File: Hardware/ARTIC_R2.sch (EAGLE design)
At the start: 114 parts, among them J1 U.FL, J2 THING_PLUS, J5 Flash Programming, K1 TLP3475R, Q1 3.1A/30V/105mΩ, U1 2Mbit SPI Flash, U2 1.8V/100mA, U3 ARTIC_R2, U4 RFPA0133, U5 AS179-92LF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

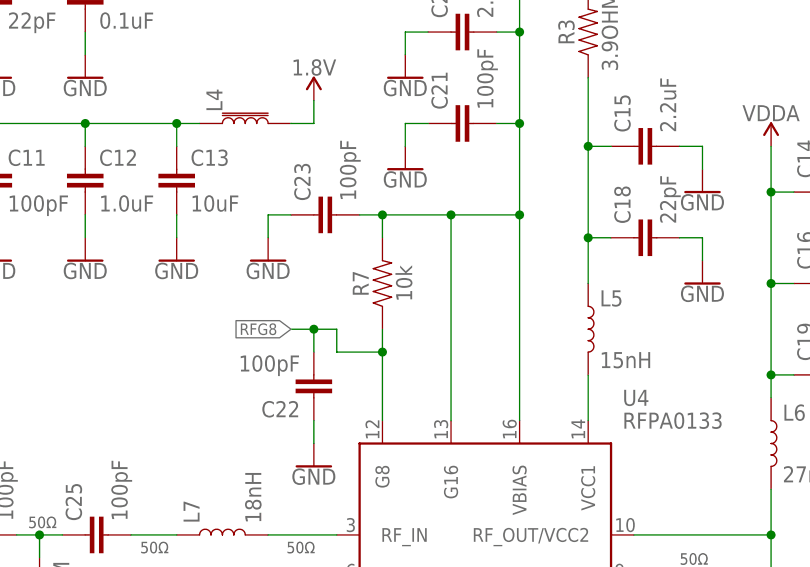
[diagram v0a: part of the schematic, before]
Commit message: Changing R7 from 10K to 1K
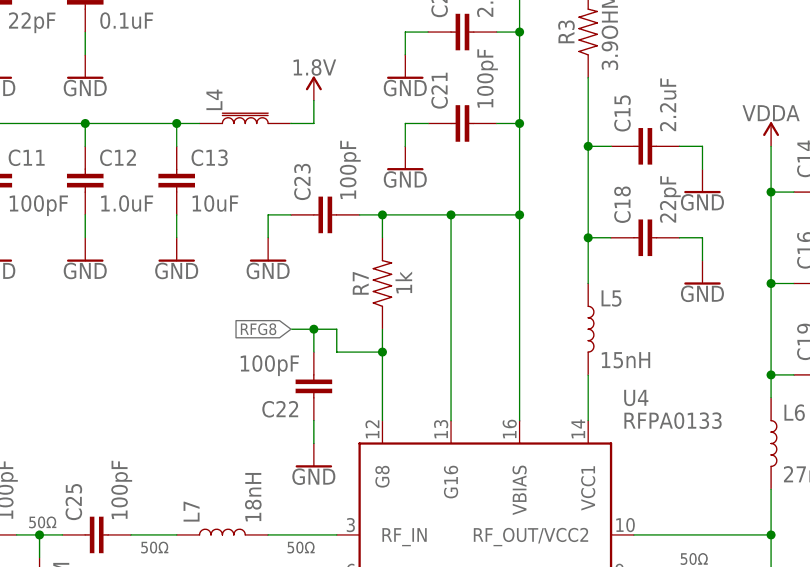
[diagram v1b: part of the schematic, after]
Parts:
- R7: value 10k -> 1k; device SparkFun-Resistors:10KOHM-0402T-1/16W-1% -> SparkFun-Resistors:1KOHM-0402T-1/16W-1%
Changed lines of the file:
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@@
 <part name="L7" library="New_Parts_Coils" deviceset="18NH" device="-0402" value="18nH"/>
 <part name="GND33" library="SparkFun-PowerSymbols" deviceset="GND" device=""/>
-<part name="R7" library="SparkFun-Resistors" deviceset="10KOHM" device="-0402T-1/16W-1%" value="10k"/>
+<part name="R7" library="SparkFun-Resistors" deviceset="1KOHM" device="-0402T-1/16W-1%" value="1k"/>
 <part name="C23" library="SparkFun-Capacitors" deviceset="100PF" device="-0402T-50V-5%" value="100pF"/>
 <part name="C22" library="SparkFun-Capacitors" deviceset="100PF" device="-0402T-50V-5%" value="100pF"/>

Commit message: Updates for X03. Design now includes a 3.0V regulator for the RF amp gain and bias.
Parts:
- removed JP7: JUMPER-SMT_2_NO_SILK, SparkFun-Jumpers:JUMPER-SMT_2_NO_SILK
- added R14: 470, New_Parts_Resistors:470OHM-0402-TIGHT-1/16W-1%
- added R17: 47, New_Parts_Resistors:47OHM-0402-TIGHT-1/16W-1%
- added TP4: TEST-POINTTP_15TH_THRU, SparkFun-Connectors:TEST-POINTTP_15TH_THRU
- added U6: 3.0V, New_Parts_IC-Power:V_REG_LP5907SOT23-3.0V
- R1, R16: value 100k -> 10k; device SparkFun-Resistors:100KOHM-0402T-1/16W-1% -> SparkFun-Resistors:10KOHM-0402T-1/16W-1%
- R7: value 1k -> 10k; device SparkFun-Resistors:1KOHM-0402T-1/16W-1% -> SparkFun-Resistors:10KOHM-0402T-1/16W-1%
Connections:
- new net PD: C43.2, C44.1, R14.2, R17.2, U4.PD
- new net VREF1: C20.2, C21.2, C23.1, K1.DRAIN_1, TP4.1, U4.G16, U4.VBIAS, U6.OUT
- net G8: no longer JP7.1
- net GND: now also C23.2, R14.1, R7.2, U6.GND; no longer C23.1, K1.DRAIN_1
- net PA_PD: now also R17.1; no longer C43.2, C44.1, U4.PD
- net RFG8: no longer JP7.2
- net VDDA: now also U6.EN, U6.IN; no longer C20.2, C21.2, C23.2, R7.2, U4.G16, U4.VBIAS
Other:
- note added: "Decoupled by C47 and C20"
- note added: "LP5907-3.0V ------------- Iout (max): 250mA Vin (max): 5.5V Vdrop (max): 250mV Iq (max): 1uA"
- note added: "Power Switching & Voltage Regulation"
- note added: "SP6214-1.8V ------------- Iout (max): 100mA Vin (max): 7.0V Vdrop (max): 250mV Iq: 65uA"
- note added: "X03"
- note removed: "1.8V Regulator"
- note removed: "Power Switching & 3.3V Regulation"
- note removed: "SP6214-1.8V ---------------- Iout (max): 100mA Vin (max): 7.0V Vdrop (max): 250mV Iq: 65uA"
- note removed: "X02"
- moved on the sheet: C1, C20, C21, C22, C23, C24, C25, C3, C4, C43, C44, C47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

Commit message: Final tweaks for X03. Changed 8dB to G8. Increased annular ring to 3.5mil.
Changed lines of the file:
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@@
 <wire x1="378.46" y1="205.74" x2="378.46" y2="279.4" width="0.2032" layer="97" style="longdash"/>
 <wire x1="99.06" y1="68.58" x2="0" y2="68.58" width="0.2032" layer="97" style="longdash"/>
-<text x="6.604" y="259.842" size="5.08" layer="97">Power Switching &amp; Voltage
+<text x="6.604" y="259.842" size="5.08" layer="94">Power Switching &amp; Voltage
 Regulation</text>
-<text x="157.48" y="213.36" size="5.08" layer="97">Flash Memory</text>
-<text x="299.72" y="213.36" size="5.08" layer="97">Antenna Switch</text>
-<text x="391.16" y="213.36" size="5.08" layer="97">Antenna</text>
-<text x="167.64" y="30.48" size="5.08" layer="97">ARTIC R2</text>
-<text x="327.66" y="81.28" size="5.08" layer="97">RF Amp</text>
-<text x="43.18" y="5.08" size="5.08" layer="97">Pins</text>
+<text x="157.48" y="213.36" size="5.08" layer="94">Flash Memory</text>
+<text x="299.72" y="213.36" size="5.08" layer="94">Antenna Switch</text>
+<text x="391.16" y="213.36" size="5.08" layer="94">Antenna</text>
+<text x="167.64" y="30.48" size="5.08" layer="94">ARTIC R2</text>
+<text x="327.66" y="81.28" size="5.08" layer="94">RF Amp</text>
+<text x="43.18" y="5.08" size="5.08" layer="94">Pins</text>
 <text x="258.572" y="82.042" size="1.27" layer="97">50Ω</text>
 <text x="285.75" y="76.962" size="1.27" layer="97">50Ω</text>
@@
 <text x="401.574" y="249.428" size="1.27" layer="97">50Ω</text>
 <wire x1="147.32" y1="205.74" x2="147.32" y2="279.4" width="0.2032" layer="97" style="longdash"/>
-<text x="117.602" y="213.614" size="5.08" layer="97">LEDs</text>
+<text x="117.602" y="213.614" size="5.08" layer="94">LEDs</text>
 <text x="330.962" y="74.168" size="1.778" layer="97" font="vector" align="top-left">RF Track Impedance: Coplanar Waveguide with Ground Calculations
 https://chemandy.com/calculators/coplanar-waveguide-with-ground-calculator.htm
@@
 20 mil track with 4 mil gap = 49.9 Ohms
 </text>
-<text x="20.32" y="78.74" size="5.08" layer="97">Gain Opto-Isolation</text>
+<text x="20.32" y="78.74" size="5.08" layer="94">Gain Opto-Isolation</text>
 <text x="207.772" y="214.122" size="1.778" layer="97">The ARTIC must be held in
 reset while programming flash</text>
